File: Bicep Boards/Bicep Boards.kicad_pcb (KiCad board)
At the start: 2 copper layers, 54.2 x 78.4 mm, 17 parts, among them J1 SM02B-SRSS-TB_LF__SN_, J11 69167-107HLF, J4 69167-107HLF, J9 87583-2010RPLF, U1 ESP32-S3-WROOM-1-N16R8, U11 TS3A5018D, U12 TS3A5018D, U4 LSM6DSMTR, U9 LP2950CZ-3.3_LFT3

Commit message: Version 2
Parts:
- moved H3 5.59 mm to (104.5, 133.0)
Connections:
- J1 pad 1: /3.7V -> GND
- J1 pad 2: GND -> /3.7V
- J9 pad 01: +3.3V -> /3.7V
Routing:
- net +3.3V: track 137.0 -> 114.3 mm
- net /3.7V: track 15.0 -> 24.6 mm
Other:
- board text removed: "J2"
- board text removed: "Left Bicep Version 1"

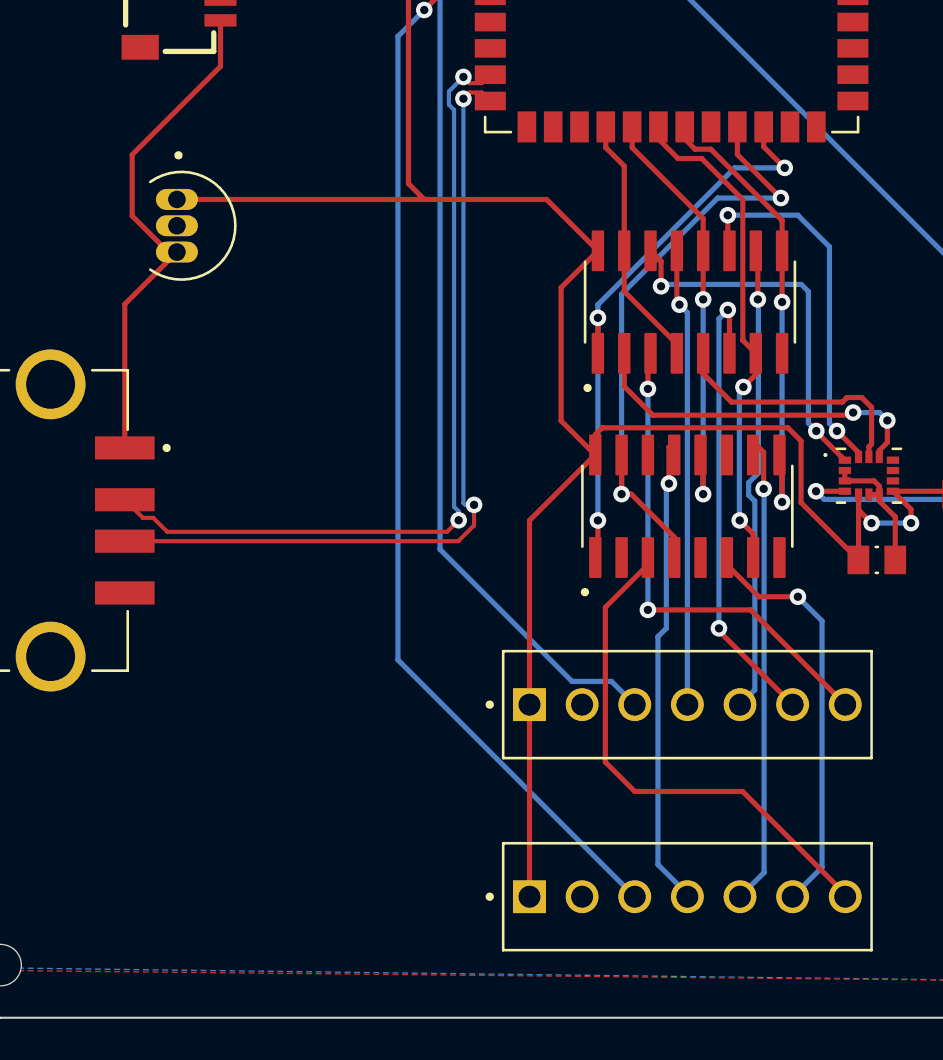
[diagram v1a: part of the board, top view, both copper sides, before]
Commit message: sensor select pin change and silk added
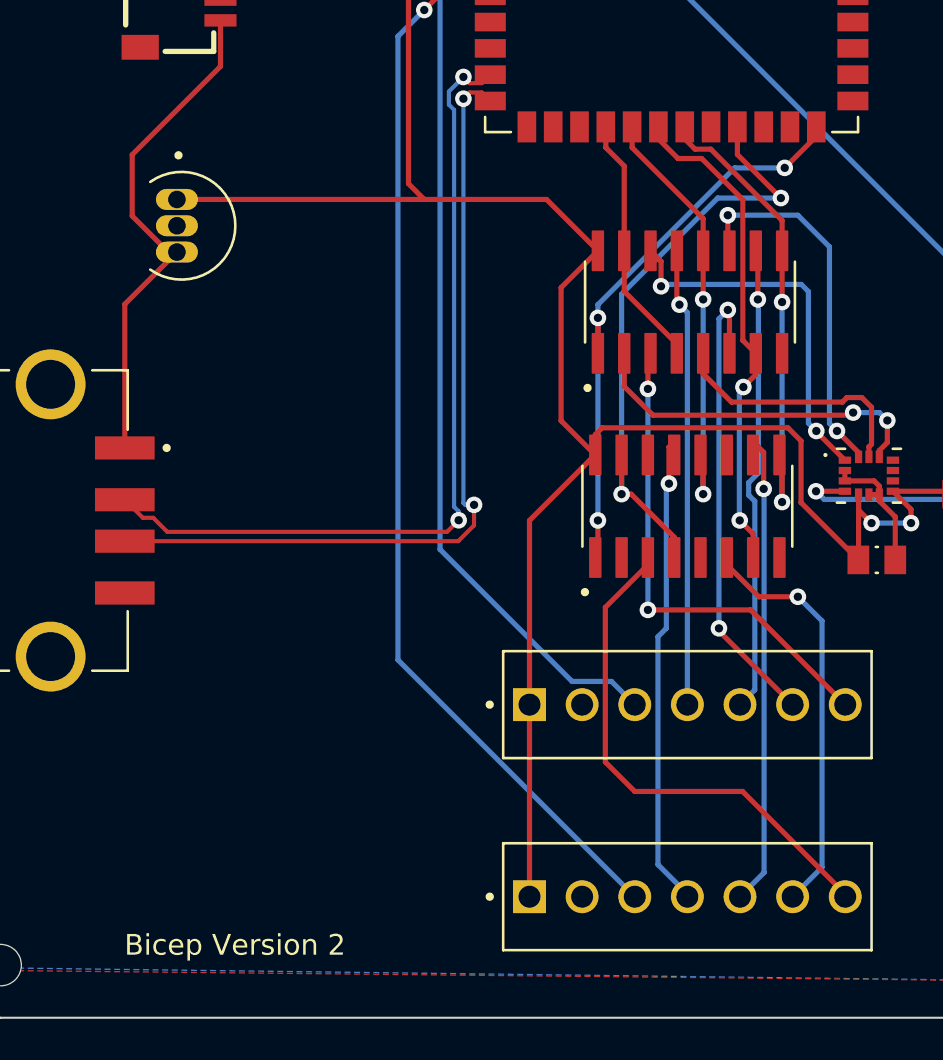
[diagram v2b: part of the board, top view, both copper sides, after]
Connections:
- U1 pad 24: SENSOR_SEL -> unconnected-(U1-IO47-Pad24)
- U1 pad 26: unconnected-(U1-IO45-Pad26) -> SENSOR_SEL
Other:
- board text added: "Bicep Version 2"
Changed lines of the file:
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@@
   (net 35 "unconnected-(U1-IO14-Pad22)")
   (net 36 "unconnected-(U1-IO48-Pad25)")
-  (net 37 "unconnected-(U1-IO45-Pad26)")
+  (net 37 "unconnected-(U1-IO47-Pad24)")
   (net 38 "unconnected-(U1-IO0-Pad27)")
   (net 39 "unconnected-(U1-IO35-Pad28)")
@@
     (property "Package" "NON STANDARD Espressif Systems")
     (property "Price" "None")
-    (property "Sheetfile" "445_Left_Bicep.kicad_sch")
+    (property "Sheetfile" "Bicep Boards.kicad_sch")
     (property "Sheetname" "")
     (property "SnapEDA_Link" "https://www.snapeda.com/parts/ESP32-S3-WROOM-1-N16R8/Espressif+Systems/view-part/?ref=snap")
@@
       (net 6 "CS2") (pinfunction "IO21") (pintype "bidirectional") (solder_mask_margin 0.102))
     (pad "24" smd rect (at 4.445 12.5) (size 0.9 1.5) (layers "F.Cu" "F.Paste" "F.Mask")
-      (net 51 "SENSOR_SEL") (pinfunction "IO47") (pintype "bidirectional") (solder_mask_margin 0.102))
+      (net 37 "unconnected-(U1-IO47-Pad24)") (pinfunction "IO47") (pintype "bidirectional+no_connect") (solder_mask_margin 0.102))
     (pad "25" smd rect (at 5.715 12.5) (size 0.9 1.5) (layers "F.Cu" "F.Paste" "F.Mask")
       (net 36 "unconnected-(U1-IO48-Pad25)") (pinfunction "IO48") (pintype "bidirectional+no_connect") (solder_mask_margin 0.102))
     (pad "26" smd rect (at 6.985 12.5) (size 0.9 1.5) (layers "F.Cu" "F.Paste" "F.Mask")
-      (net 37 "unconnected-(U1-IO45-Pad26)") (pinfunction "IO45") (pintype "bidirectional+no_connect") (solder_mask_margin 0.102))
+      (net 51 "SENSOR_SEL") (pinfunction "IO45") (pintype "bidirectional") (solder_mask_margin 0.102))
     (pad "27" smd rect (at 8.75 11.25) (size 1.5 0.9) (layers "F.Cu" "F.Paste" "F.Mask")
       (net 38 "unconnected-(U1-IO0-Pad27)") (pinfunction "IO0") (pintype "bidirectional+no_connect") (solder_mask_margin 0.102))
@@
     (property "Purchase-URL" "https://www.snapeda.com/api/url_track_click_mouser/?unipart_id=9742722&manufacturer=Amphenol CS (FCI)&part_name=69167-107HLF&search_term=69167-107hlf")
     (property "STANDARD" "Manufacturer Recommendations")
-    (property "Sheetfile" "445_Left_Bicep.kicad_sch")
+    (property "Sheetfile" "Bicep Boards.kicad_sch")
     (property "Sheetname" "")
     (property "SnapEDA_Link" "https://www.snapeda.com/parts/69167-107HLF/Amphenol+FCI/view-part/?ref=snap")
@@
     (property "Package" "None")
     (property "Price" "None")
-    (property "Sheetfile" "445_Left_Bicep.kicad_sch")
+    (property "Sheetfile" "Bicep Boards.kicad_sch")
     (property "Sheetname" "")
     (property "SnapEDA_Link" "https://www.snapeda.com/parts/SM02B-SRSS-TB(LF)(SN)/JST+Sales+America+Inc./view-part/?ref=snap")
@@
     (property "Purchase-URL" "https://www.snapeda.com/api/url_track_click_mouser/?unipart_id=349302&manufacturer=Texas Instruments&part_name=TS3A5018D&search_term=ts3a5018")
     (property "STANDARD" "IPC-7351B")
-    (property "Sheetfile" "445_Left_Bicep.kicad_sch")
+    (property "Sheetfile" "Bicep Boards.kicad_sch")
     (property "Sheetname" "")
     (property "SnapEDA_Link" "https://www.snapeda.com/parts/TS3A5018D/Texas+Instruments/view-part/?ref=snap")
@@
     (descr "Mounting Hole 2mm, no annular")
     (tags "mounting hole 2mm no annular")
-    (property "Sheetfile" "445_Left_Bicep.kicad_sch")
+    (property "Sheetfile" "Bicep Boards.kicad_sch")
     (property "Sheetname" "")
     (property "ki_description" "Mounting Hole without connection")
@@
     (property "Price" "None")
     (property "Purchase-URL" "https://www.snapeda.com/api/url_track_click_mouser/?unipart_id=1079240&manufacturer=Texas Instruments&part_name=LP2950CZ-3.3/LFT3&search_term= lp2950cz")
-    (property "Sheetfile" "445_Left_Bicep.kicad_sch")
+    (property "Sheetfile" "Bicep Boards.kicad_sch")
     (property "Sheetname" "")
     (property "SnapEDA_Link" "https://www.snapeda.com/parts/LP2950CZ-3.3/LFT3/Texas+Instruments/view-part/?ref=snap")
@@
     (descr "Mounting Hole 2mm, no annular")
     (tags "mounting hole 2mm no annular")
-    (property "Sheetfile" "445_Left_Bicep.kicad_sch")
+    (property "Sheetfile" "Bicep Boards.kicad_sch")
     (property "Sheetname" "")
     (property "ki_description" "Mounting Hole without connection")
@@
     (property "Purchase-URL" "https://www.snapeda.com/api/url_track_click_mouser/?unipart_id=9742722&manufacturer=Amphenol CS (FCI)&part_name=69167-107HLF&search_term=69167-107hlf")
     (property "STANDARD" "Manufacturer Recommendations")
-    (property "Sheetfile" "445_Left_Bicep.kicad_sch")
+    (property "Sheetfile" "Bicep Boards.kicad_sch")
     (property "Sheetname" "")
     (property "SnapEDA_Link" "https://www.snapeda.com/parts/69167-107HLF/Amphenol+FCI/view-part/?ref=snap")
@@
   (footprint "ECE 445 Footprints:AC-903-D-1P" (layer "F.Cu")
     (at 115.062 69.882)
-    (property "Sheetfile" "445_Left_Bicep.kicad_sch")
+    (property "Sheetfile" "Bicep Boards.kicad_sch")
     (property "Sheetname" "")
     (property "ki_description" "Buzzer, polarized")
@@
     (property "Purchase-URL" "https://www.snapeda.com/api/url_track_click_mouser/?unipart_id=3822774&manufacturer=Amphenol ICC&part_name=87583-2010RPLF&search_term=87583-2010rplf")
     (property "STANDARD" "Manufacturer Recommendations")
-    (property "Sheetfile" "445_Left_Bicep.kicad_sch")
+    (property "Sheetfile" "Bicep Boards.kicad_sch")
     (property "Sheetname" "")
     (property "SnapEDA_Link" "https://www.snapeda.com/parts/87583-2010RPLF/Amphenol+FCI/view-part/?ref=snap")
@@
   (footprint "CL21F104ZAANNNC:CAPC2012X135N" (layer "F.Cu")
     (at 151.384 110.236)
-    (property "Sheetfile" "445_Left_Bicep.kicad_sch")
+    (property "Sheetfile" "Bicep Boards.kicad_sch")
     (property "Sheetname" "")
     (property "ki_description" "Unpolarized capacitor, small symbol")
@@
     (property "Purchase-URL" "https://www.snapeda.com/api/url_track_click_mouser/?unipart_id=581716&manufacturer=STMicroelectronics&part_name=LSM6DSMTR&search_term=None")
     (property "STANDARD" "IPC 7351B")
-    (property "Sheetfile" "445_Left_Bicep.kicad_sch")
+    (property "Sheetfile" "Bicep Boards.kicad_sch")
     (property "Sheetname" "")
     (property "SnapEDA_Link" "https://www.snapeda.com/parts/LSM6DSMTR/STMicroelectronics/view-part/?ref=snap")
@@
   (footprint "CL21F104ZAANNNC:CAPC2012X135N" (layer "F.Cu")
     (at 146.812 113.411 180)
-    (property "Sheetfile" "445_Left_Bicep.kicad_sch")
+    (property "Sheetfile" "Bicep Boards.kicad_sch")
     (property "Sheetname" "")
     (property "ki_description" "Unpolarized capacitor, small symbol")
@@
     (descr "Mounting Hole 2mm, no annular")
     (tags "mounting hole 2mm no annular")
-    (property "Sheetfile" "445_Left_Bicep.kicad_sch")
+    (property "Sheetfile" "Bicep Boards.kicad_sch")
     (property "Sheetname" "")
     (property "ki_description" "Mounting Hole without connection")
@@
     (descr "Mounting Hole 2mm, no annular")
     (tags "mounting hole 2mm no annular")
-    (property "Sheetfile" "445_Left_Bicep.kicad_sch")
+    (property "Sheetfile" "Bicep Boards.kicad_sch")
     (property "Sheetname" "")
     (property "ki_description" "Mounting Hole without connection")
@@
   (footprint "RMCF0805JG10K0:RESC2012X65N" (layer "F.Cu")
     (at 121.031 81.788 -90)
-    (property "Sheetfile" "445_Left_Bicep.kicad_sch")
+    (property "Sheetfile" "Bicep Boards.kicad_sch")
     (property "Sheetname" "")
     (property "ki_description" "Resistor")
@@
     (property "Purchase-URL" "https://www.snapeda.com/api/url_track_click_mouser/?unipart_id=349302&manufacturer=Texas Instruments&part_name=TS3A5018D&search_term=ts3a5018")
     (property "STANDARD" "IPC-7351B")
-    (property "Sheetfile" "445_Left_Bicep.kicad_sch")
+    (property "Sheetfile" "Bicep Boards.kicad_sch")
     (property "Sheetname" "")
     (property "SnapEDA_Link" "https://www.snapeda.com/parts/TS3A5018D/Texas+Instruments/view-part/?ref=snap")
@@
   (gr_line (start 156.21 132.969) (end 156.21 59.69)
     (stroke (width 0.1) (type default)) (layer "Edge.Cuts"))
+  (gr_text "Bicep Version 2" (at 110.49 132.588) (layer "F.SilkS")
+    (effects (font (size 1 1) (thickness 0.15)) (justify left bottom))
+  )
   (segment (start 126.672 76.02) (end 124.206 78.486) (width 0.25) (layer "F.Cu") (net 1))
   (segment (start 113.03 96.012) (end 124.968 96.012) (width 0.25) (layer "F.Cu") (net 1))
@@
   (segment (start 146.939 106.299) (end 147.32 106.68) (width 0.25) (layer "B.Cu") (net 28))
   (segment (start 133.35 111.506) (end 133.35 113.168) (width 0.25) (layer "F.Cu") (net 51))
-  (segment (start 141.351 93.472) (end 141.351 92.51) (width 0.25) (layer "F.Cu") (net 51))
-  (segment (start 142.367 94.488) (end 141.351 93.472) (width 0.25) (layer "F.Cu") (net 51))
+  (segment (start 142.367 94.488) (end 143.891 92.964) (width 0.25) (layer "F.Cu") (net 51))
   (segment (start 133.35 113.168) (end 133.223 113.295) (width 0.25) (layer "F.Cu") (net 51))
+  (segment (start 143.891 92.964) (end 143.891 92.51) (width 0.25) (layer "F.Cu") (net 51))
   (segment (start 133.35 103.44) (end 133.35 101.727) (width 0.25) (layer "F.Cu") (net 51))
   (via (at 133.35 111.506) (size 0.8) (drill 0.4) (layers "F.Cu" "B.Cu") (net 51))
